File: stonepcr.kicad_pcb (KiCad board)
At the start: 2 copper layers, 242.1 x 134 mm, 51 parts, among them J1 ATX-24, J10 Conn_01x05, J11 Conn_01x05, J12 Conn_01x02, J13 Conn_01x09, J14 Conn_01x03, J15 Conn_01x03, J2 Conn_01x02, J3 Conn_01x02, J4 Conn_ARM_JTAG_SWD_10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

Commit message: Preparation for differential routing and small placement corrections.
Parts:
- J8: footprint Connector_USB:USB_Micro-B_Molex-105017-0001 -> Connector_USB:USB_Micro-B_Wuerth_629105150521
- moved J11 108.3 mm to (193.9, 130.1)
- moved U4 108.3 mm to (125.6, 114.7)
- moved J13 108.3 mm to (119.7, 114.5)
- moved J15 75.5 mm to (72.5, 59.1)
- moved J14 75.2 mm to (68.6, 59.1)
- moved R10 21.0 mm to (82.4, 80.9), turned to 90 degrees
- moved Y2 16.3 mm to (86.4, 85.8), turned to 90 degrees
- moved C2 15.5 mm to (86.3, 102.8), turned to 0 degrees
- moved C1 14.3 mm to (81.3, 100.8), turned to 270 degrees
- moved C3 13.0 mm to (82.4, 85.5), turned to 270 degrees
- moved J7 10.2 mm to (77.0, 70.6)
- moved C4 9.24 mm to (86.4, 89.5), turned to 180 degrees
- moved Y1 7.00 mm to (86.4, 99.5), turned to 90 degrees
- moved C5 5.94 mm to (77.6, 78.8)
- moved J4 4.87 mm to (82.0, 52.2)
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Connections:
- net /ControllerSchematic/OSC_IN_HSE renamed /ControllerSchematic/OSC_HSE+
- net /ControllerSchematic/OSC_IN_LSE renamed /ControllerSchematic/OSC_LSE+
- net /ControllerSchematic/OSC_OUT_HSE renamed /ControllerSchematic/OSC_HSE-
- net /ControllerSchematic/OSC_OUT_LSE renamed /ControllerSchematic/OSC_LSE-
- net /ControllerSchematic/USB_DATA_MINUS renamed /ControllerSchematic/USB_DATA-
- net /ControllerSchematic/USB_DATA_PLUS renamed /ControllerSchematic/USB_DATA+
- net Net-(J8-Pad2) renamed /InterfacesSchematic/D-
- net Net-(J8-Pad3) renamed /InterfacesSchematic/D+
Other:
- board size 242.1 x 134 mm -> 166.1 x 103.2 mm

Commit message: Trackeo
Pobre trackeo parcial. Backup
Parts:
- R7: value 1k -> 10k
- moved R11 72.9 mm to (103.0, 67.0), turned to 0 degrees
- moved R7 71.8 mm to (103.0, 56.7), turned to 0 degrees
- moved R12 70.2 mm to (103.0, 61.7), turned to 180 degrees
- moved D3 69.2 mm to (99.4, 61.7), turned to 180 degrees
- moved D2 68.0 mm to (99.4, 67.0), turned to 180 degrees
- moved D1 66.7 mm to (99.4, 56.7), turned to 180 degrees
- moved J4 64.5 mm to (40.5, 101.6), turned to 0 degrees
- moved J14 1.23 mm to (68.9, 57.9)
- moved J15 1.23 mm to (72.8, 57.9)
- turned C2 to 180 degrees
- turned R8 to 180 degrees
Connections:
- net Net-(J2-Pad1) renamed /PeltierSchematic/OUT1+
- net Net-(J2-Pad2) renamed /PeltierSchematic/OUT1-
- net Net-(J3-Pad1) renamed /PeltierSchematic/OUT2+
- net Net-(J3-Pad2) renamed /PeltierSchematic/OUT2-
- SW2 pad 1: +5V -> +3V3
- SW3 pad 1: +5V -> +3V3
- U1 pad 12: +12V -> +3V3
- U1 pad 13: +3V3 -> +12V
- U1 pad 23: +3V3 -> +12V
- U1 pad 3: +3V3 -> +12V
- U1 pad 31: +3V3 -> +12V
- U2 pad 12: +12V -> +3V3
- U2 pad 13: +3V3 -> +12V
- U2 pad 23: +3V3 -> +12V
- U2 pad 3: +3V3 -> +12V
- U2 pad 31: +3V3 -> +12V
- U3 pad 24: /ControllerSchematic/THERMISTOR_IN_1 -> /ControllerSchematic/THERMISTOR_IN_2
- U3 pad 25: /ControllerSchematic/THERMISTOR_IN_2 -> /ControllerSchematic/THERMISTOR_IN_1
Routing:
- net GND: track 0.00 -> 262.1 mm
- net +3V3: track 0.00 -> 192.3 mm
- net +12V: track 0.00 -> 80.5 mm
- net /ControllerSchematic/RST: track 0.00 -> 64.0 mm, vias 0 -> 1
- net /ControllerSchematic/VENTILADOR_PWM_1: track 0.00 -> 38.5 mm, vias 0 -> 1
- net /ControllerSchematic/SCREEN_RESET: track 0.00 -> 32.4 mm, vias 0 -> 1
- net /ControllerSchematic/SWDIO: track 0.00 -> 30.2 mm, vias 0 -> 1
- net /ControllerSchematic/VENTILADOR_PWM_2: track 0.00 -> 29.2 mm, vias 0 -> 1
- net /ControllerSchematic/SWO: track 0.00 -> 27.9 mm
- net /InterfacesSchematic/D+: track 0.00 -> 23.1 mm
- net /ControllerSchematic/THERMISTOR_IN_2: track 0.00 -> 22.7 mm
- net /ControllerSchematic/SD_CS_SPI: track 0.00 -> 22.4 mm, vias 0 -> 1
- net /InterfacesSchematic/D-: track 0.00 -> 22.2 mm
- net /ControllerSchematic/PELTIER_EN_1: track 0.00 -> 21.2 mm
- net /ControllerSchematic/SWDCLK: track 0.00 -> 20.8 mm
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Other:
- net class POWER added: clearance 0.2, trace_width 2, via_dia 1, via_drill 0.4

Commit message: Replacement and adjustments
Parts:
- J8: moved to B.Cu
- moved J8 5.15 mm to (37.7, 88.0), turned to 90 degrees
- moved BZ1 1.78 mm to (43.0, 73.8)
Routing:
- net GND: track 262.1 -> 0.00 mm
- net +3V3: track 192.3 -> 0.00 mm
- net +12V: track 80.5 -> 0.00 mm
- net /ControllerSchematic/RST: track 64.0 -> 0.00 mm, vias 1 -> 0
- net /ControllerSchematic/VENTILADOR_PWM_1: track 38.5 -> 0.00 mm, vias 1 -> 0
- net /ControllerSchematic/SCREEN_RESET: track 32.4 -> 0.00 mm, vias 1 -> 0
- net /ControllerSchematic/SWDIO: track 30.2 -> 0.00 mm, vias 1 -> 0
- net /ControllerSchematic/VENTILADOR_PWM_2: track 29.2 -> 0.00 mm, vias 1 -> 0
- net /ControllerSchematic/SWO: track 27.9 -> 0.00 mm
- net /InterfacesSchematic/D+: track 23.1 -> 0.00 mm
- net /ControllerSchematic/THERMISTOR_IN_2: track 22.7 -> 0.00 mm
- net /ControllerSchematic/SD_CS_SPI: track 22.4 -> 0.00 mm, vias 1 -> 0
- net /InterfacesSchematic/D-: track 22.2 -> 0.00 mm
- net /ControllerSchematic/PELTIER_EN_1: track 21.2 -> 0.00 mm
- net /ControllerSchematic/SWDCLK: track 20.8 -> 0.00 mm
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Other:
- board size 166.1 x 103.2 mm -> 166.6 x 102.5 mm

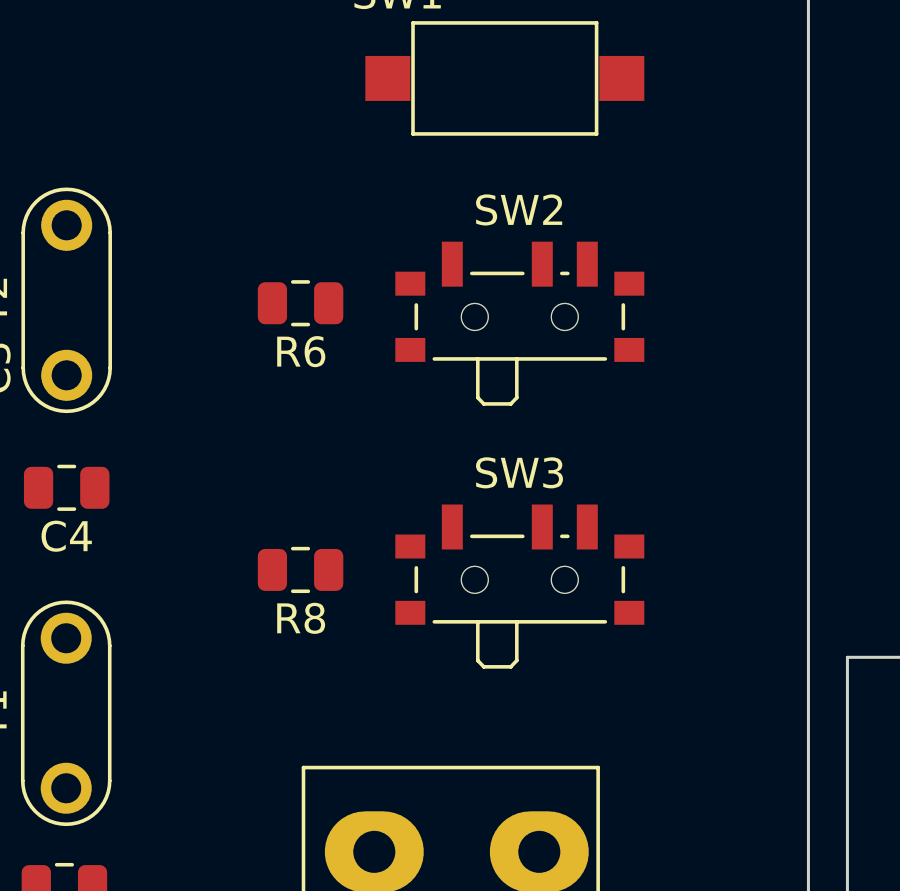
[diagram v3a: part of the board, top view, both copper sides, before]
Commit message: Rotación Swithc
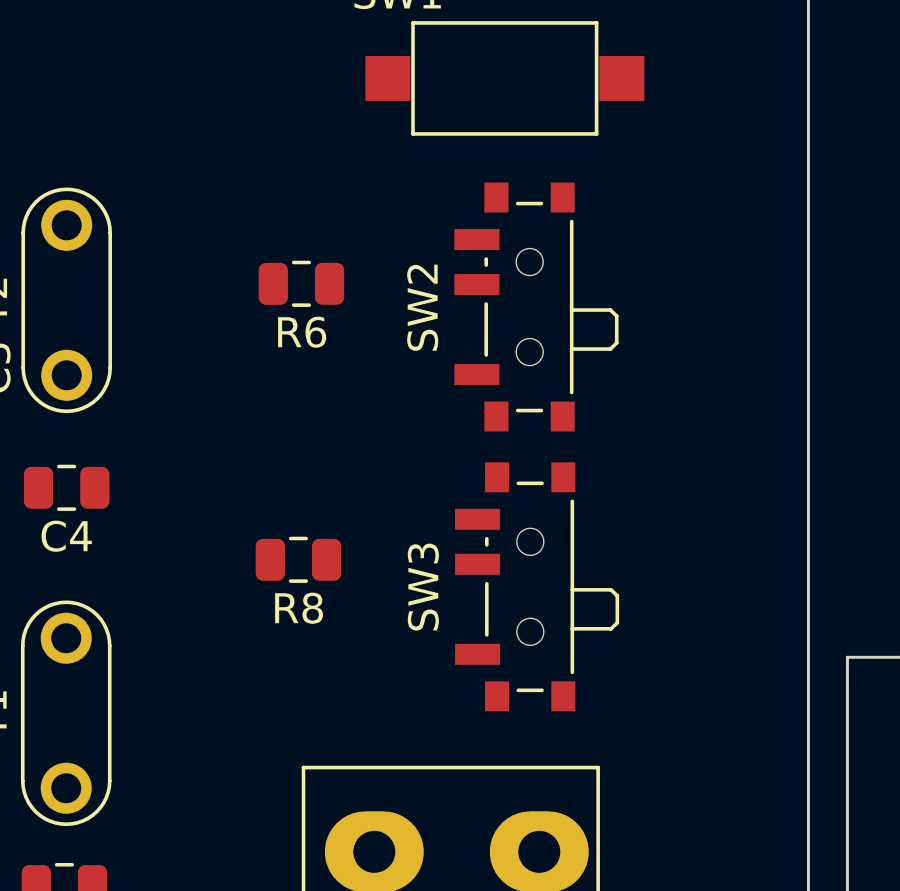
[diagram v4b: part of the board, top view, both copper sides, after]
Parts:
- moved R6 0.65 mm to (94.2, 82.7)
- moved SW3 0.56 mm to (101.5, 92.8), turned to 90 degrees
- moved R8 0.34 mm to (94.1, 91.9)
- turned SW2 to 90 degrees

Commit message: Initial Routing
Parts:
- moved J9 15.1 mm to (35.8, 64.3)
- moved C5 12.9 mm to (90.1, 75.7)
- moved BZ1 12.7 mm to (43.8, 61.1)
- moved R3 12.3 mm to (47.5, 54.5)
- moved C4 9.51 mm to (82.4, 80.9), turned to 270 degrees
- moved C2 8.66 mm to (81.6, 95.5), turned to 270 degrees
- moved J12 8.33 mm to (50.7, 66.8), turned to 180 degrees
- moved J10 5.99 mm to (49.2, 70.7), turned to 90 degrees
- moved C10 5.45 mm to (75.2, 92.3)
- moved J4 4.54 mm to (37.2, 98.5), turned to 270 degrees
- moved R10 3.74 mm to (82.4, 77.2), turned to 0 degrees
- moved R9 3.49 mm to (81.6, 91.9), turned to 0 degrees
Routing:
- net /ControllerSchematic/PELTIER_EN_2: track 0.00 -> 51.7 mm, vias 0 -> 6
- net /ControllerSchematic/JTDI: track 0.00 -> 49.6 mm, vias 0 -> 2
- net /ControllerSchematic/BOOT0: track 0.00 -> 48.5 mm, vias 0 -> 4
- net /ControllerSchematic/PELTIER_EN_1: track 0.00 -> 47.9 mm, vias 0 -> 4
- net /ControllerSchematic/SWO: track 0.00 -> 47.1 mm, vias 0 -> 2
- net /ControllerSchematic/SWDCLK: track 0.00 -> 40.8 mm, vias 0 -> 2
- net /ControllerSchematic/PELTIER_IN_B_2: track 0.00 -> 37.7 mm, vias 0 -> 3
- net /ControllerSchematic/PELTIER_IN_A_1: track 0.00 -> 35.7 mm, vias 0 -> 4
- net +12V: track 0.00 -> 35.6 mm
- net /ControllerSchematic/PELTIER_PWM_2: track 0.00 -> 33.6 mm, vias 0 -> 4
- net /ControllerSchematic/PELTIER_PWM_1: track 0.00 -> 31.1 mm, vias 0 -> 2
- net /ControllerSchematic/PELTIER_IN_A_2: track 0.00 -> 29.2 mm, vias 0 -> 2
- net /ControllerSchematic/PELTIER_IN_B_1: track 0.00 -> 28.9 mm, vias 0 -> 2
- net /ControllerSchematic/OSC_LSE+: track 0.00 -> 25.2 mm, vias 0 -> 2
- net /ControllerSchematic/OSC_HSE-: track 0.00 -> 20.2 mm, vias 0 -> 2
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
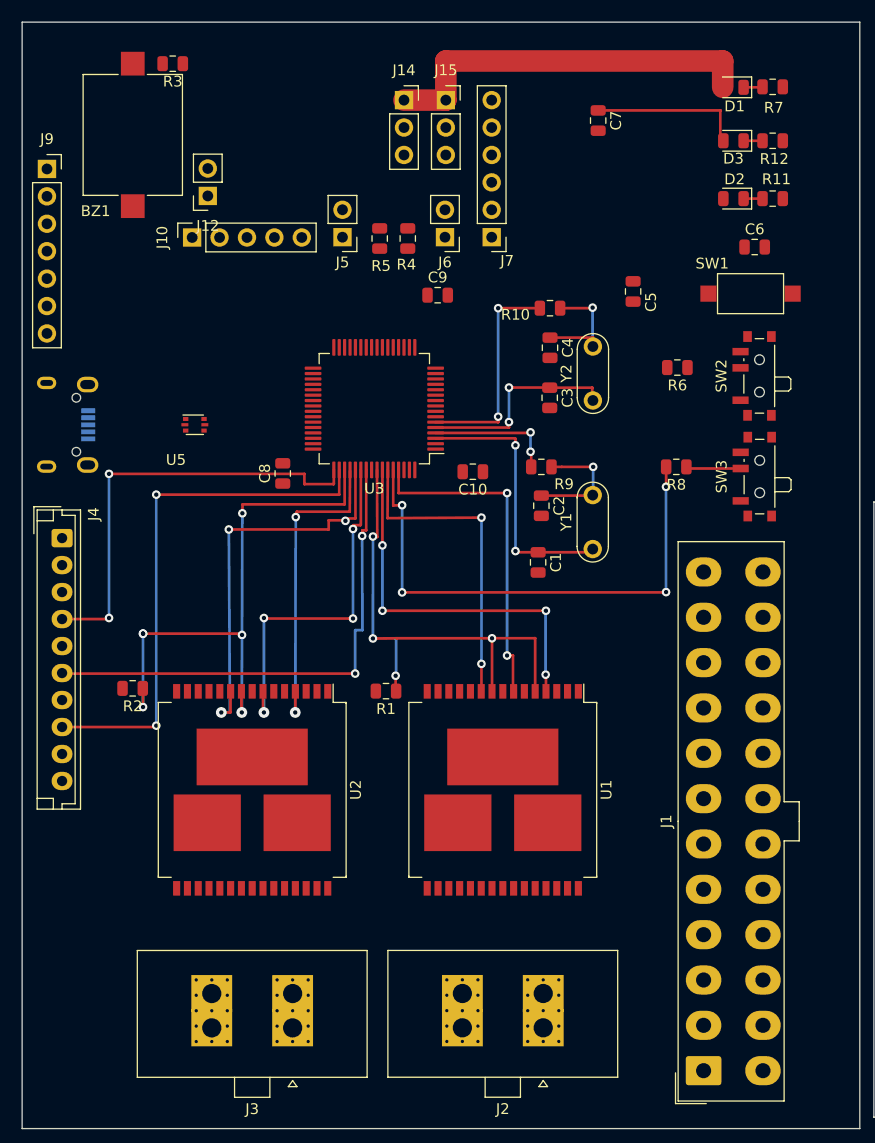
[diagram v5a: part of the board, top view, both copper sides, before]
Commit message: Removal of LED 5V and further routing
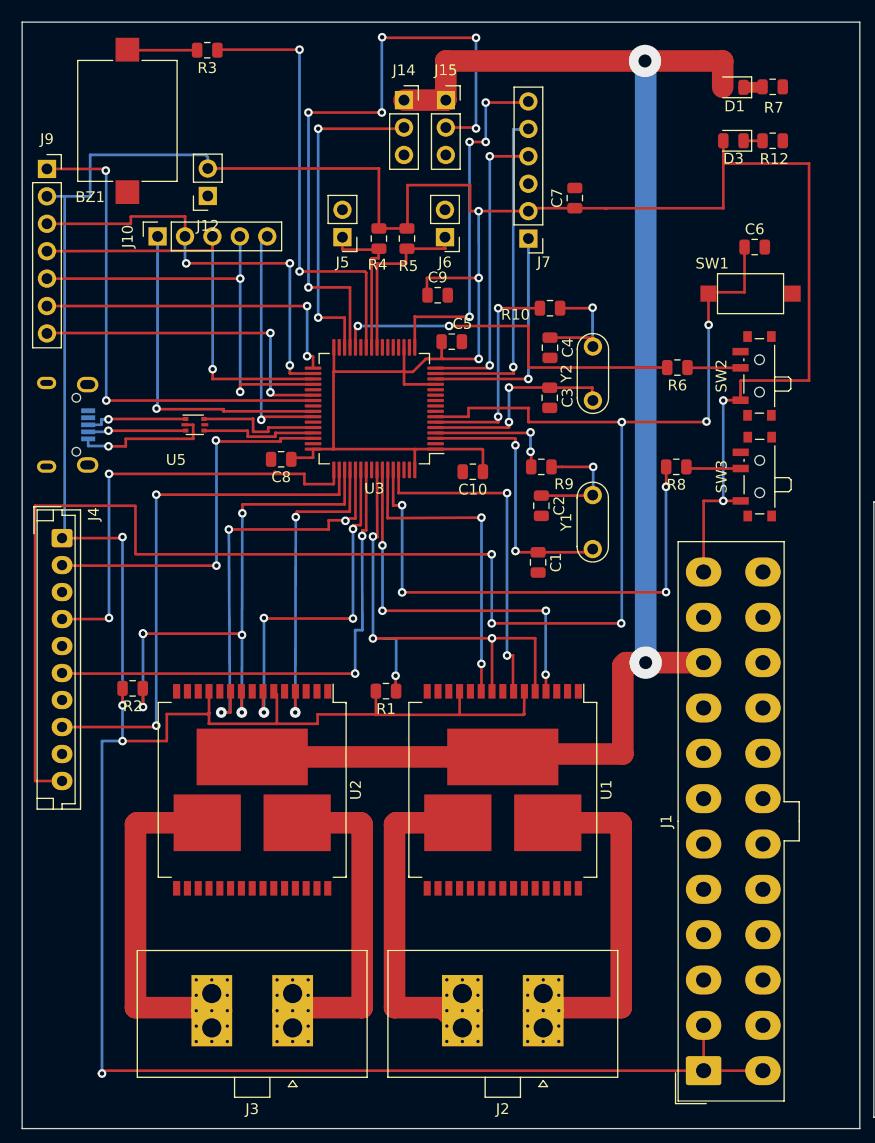
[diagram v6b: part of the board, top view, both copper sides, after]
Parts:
- removed D2: LED, LED_SMD:LED_0805_2012Metric
- removed R11: 1k, Resistor_SMD:R_0805_2012Metric
- moved C5 17.4 mm to (73.3, 80.3), turned to 0 degrees
- moved C7 7.50 mm to (84.7, 67.0), turned to 90 degrees
- moved R3 3.44 mm to (50.6, 53.3)
- moved J7 3.40 mm to (80.4, 70.8)
- moved J10 3.20 mm to (46.0, 70.5)
- moved R4 2.67 mm to (66.5, 70.8)
- moved R5 2.53 mm to (69.2, 70.8)
- moved BZ1 1.39 mm to (43.2, 59.9)
- moved C8 1.32 mm to (57.5, 91.2), turned to 180 degrees
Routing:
- net +3V3: track 14.2 -> 427.7 mm, vias 0 -> 9
- net /ControllerSchematic/RST: track 0.00 -> 158.6 mm, vias 0 -> 6
- net +12V: track 35.6 -> 141.4 mm, vias 0 -> 2
- net /ControllerSchematic/VENTILADOR_PWM_1: track 0.00 -> 59.7 mm, vias 0 -> 6
- net /ControllerSchematic/SCREEN_RESET: track 0.00 -> 46.3 mm, vias 0 -> 2
- net /ControllerSchematic/BUZZER_PWM_IN: track 0.00 -> 41.3 mm, vias 0 -> 2
- net /ControllerSchematic/SPI_CLOCK_IN: track 0.00 -> 39.9 mm, vias 0 -> 3
- net /DisplaySchematic/MOSI_IN: track 0.00 -> 39.8 mm, vias 0 -> 2
- net /DisplaySchematic/MISO_IN: track 0.00 -> 39.2 mm, vias 0 -> 1
- net /ControllerSchematic/SWDIO: track 0.00 -> 35.6 mm, vias 0 -> 2
- net /ControllerSchematic/BOOT1: track 0.00 -> 34.6 mm, vias 0 -> 2
- net /ControllerSchematic/BT_STATE: track 0.00 -> 33.3 mm, vias 0 -> 4
- net /PeltierSchematic/OUT1+: track 0.00 -> 31.6 mm
- net /PeltierSchematic/OUT2-: track 0.00 -> 31.3 mm
- net /ControllerSchematic/BT_RXD: track 0.00 -> 31.3 mm, vias 0 -> 1
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
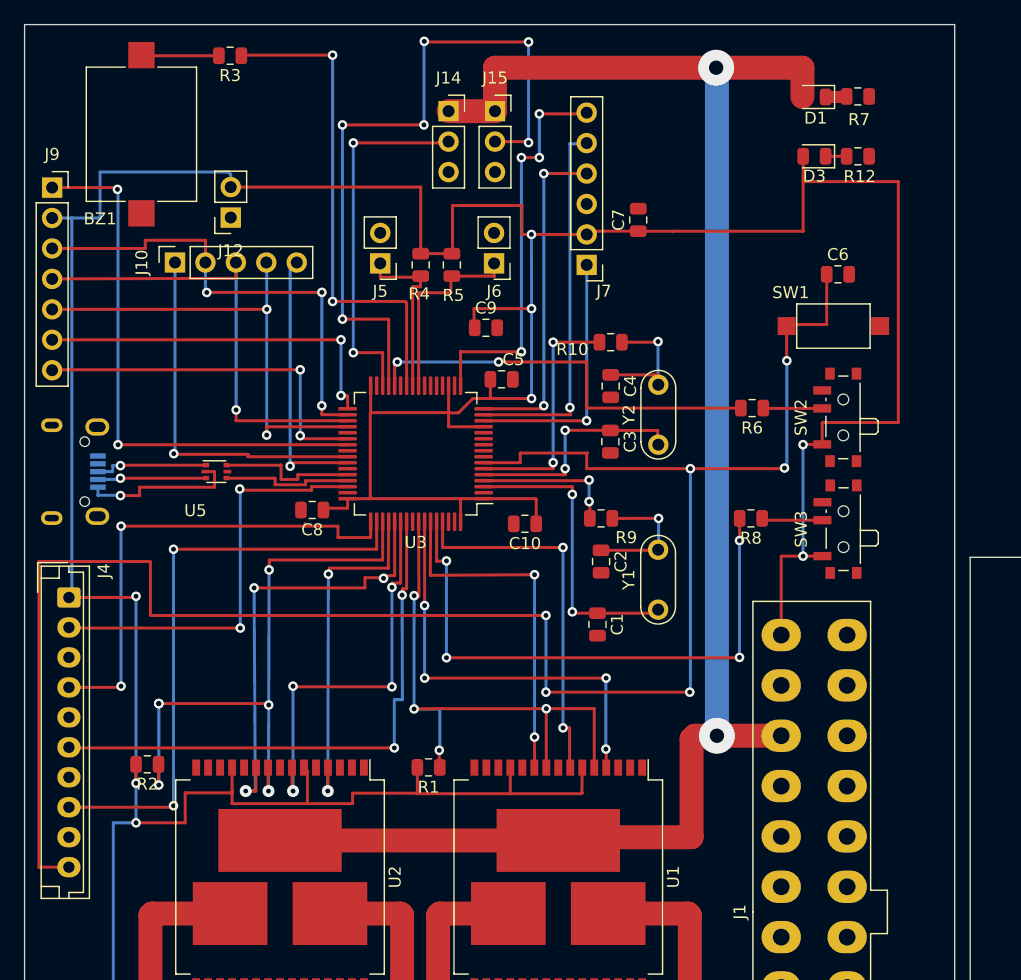
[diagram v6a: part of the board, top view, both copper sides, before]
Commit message: Copper layer for logic
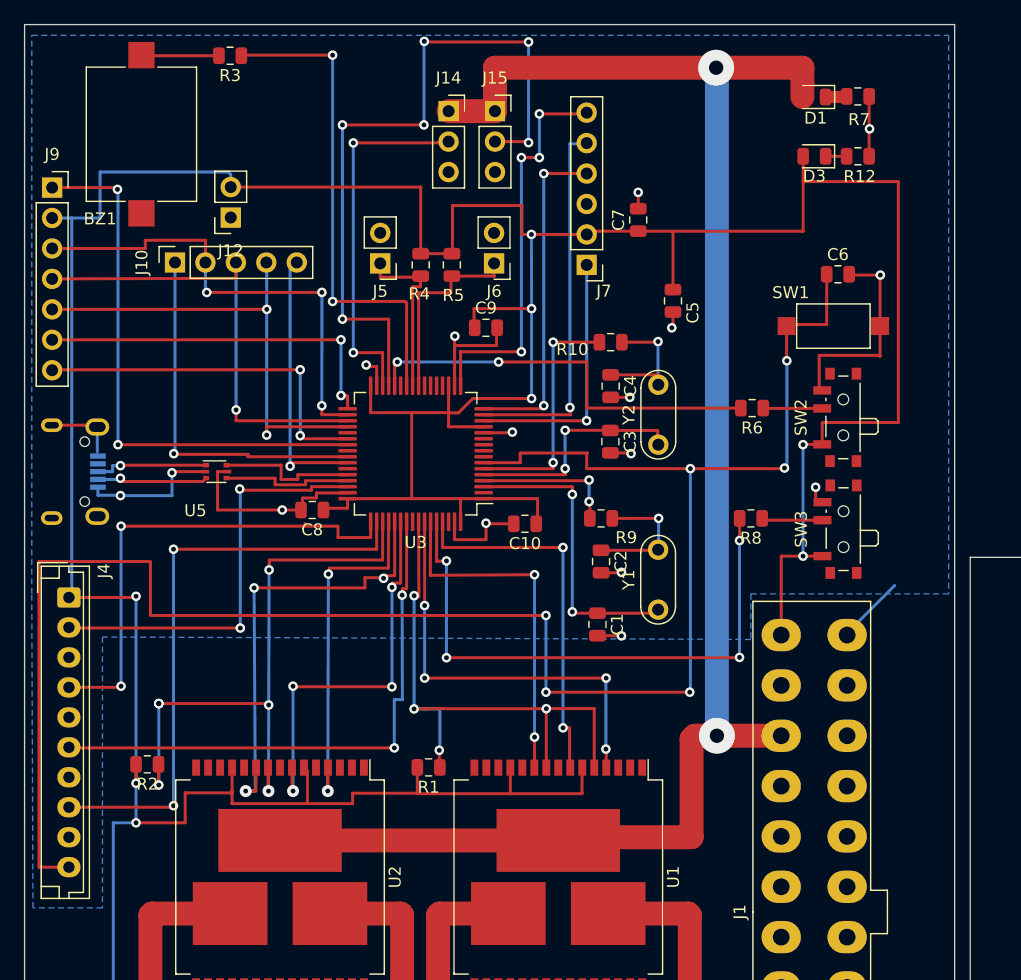
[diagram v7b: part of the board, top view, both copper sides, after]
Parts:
- moved C5 15.7 mm to (87.6, 73.8), turned to 270 degrees
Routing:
- net GND: track 0.42 -> 83.9 mm, vias 0 -> 14
- net +3V3: track 427.7 -> 430.9 mm
- net VBUS: track 13.2 -> 11.6 mm, vias 1 -> 2
- added copper zone on B.Cu, net GND
